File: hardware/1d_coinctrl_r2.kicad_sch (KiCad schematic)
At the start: 14 parts, among them J1 +12V INPUT, J2 CO LINE, J3 V_RLY_SEL, J5 COIN LINE, J7 Conn_01x02

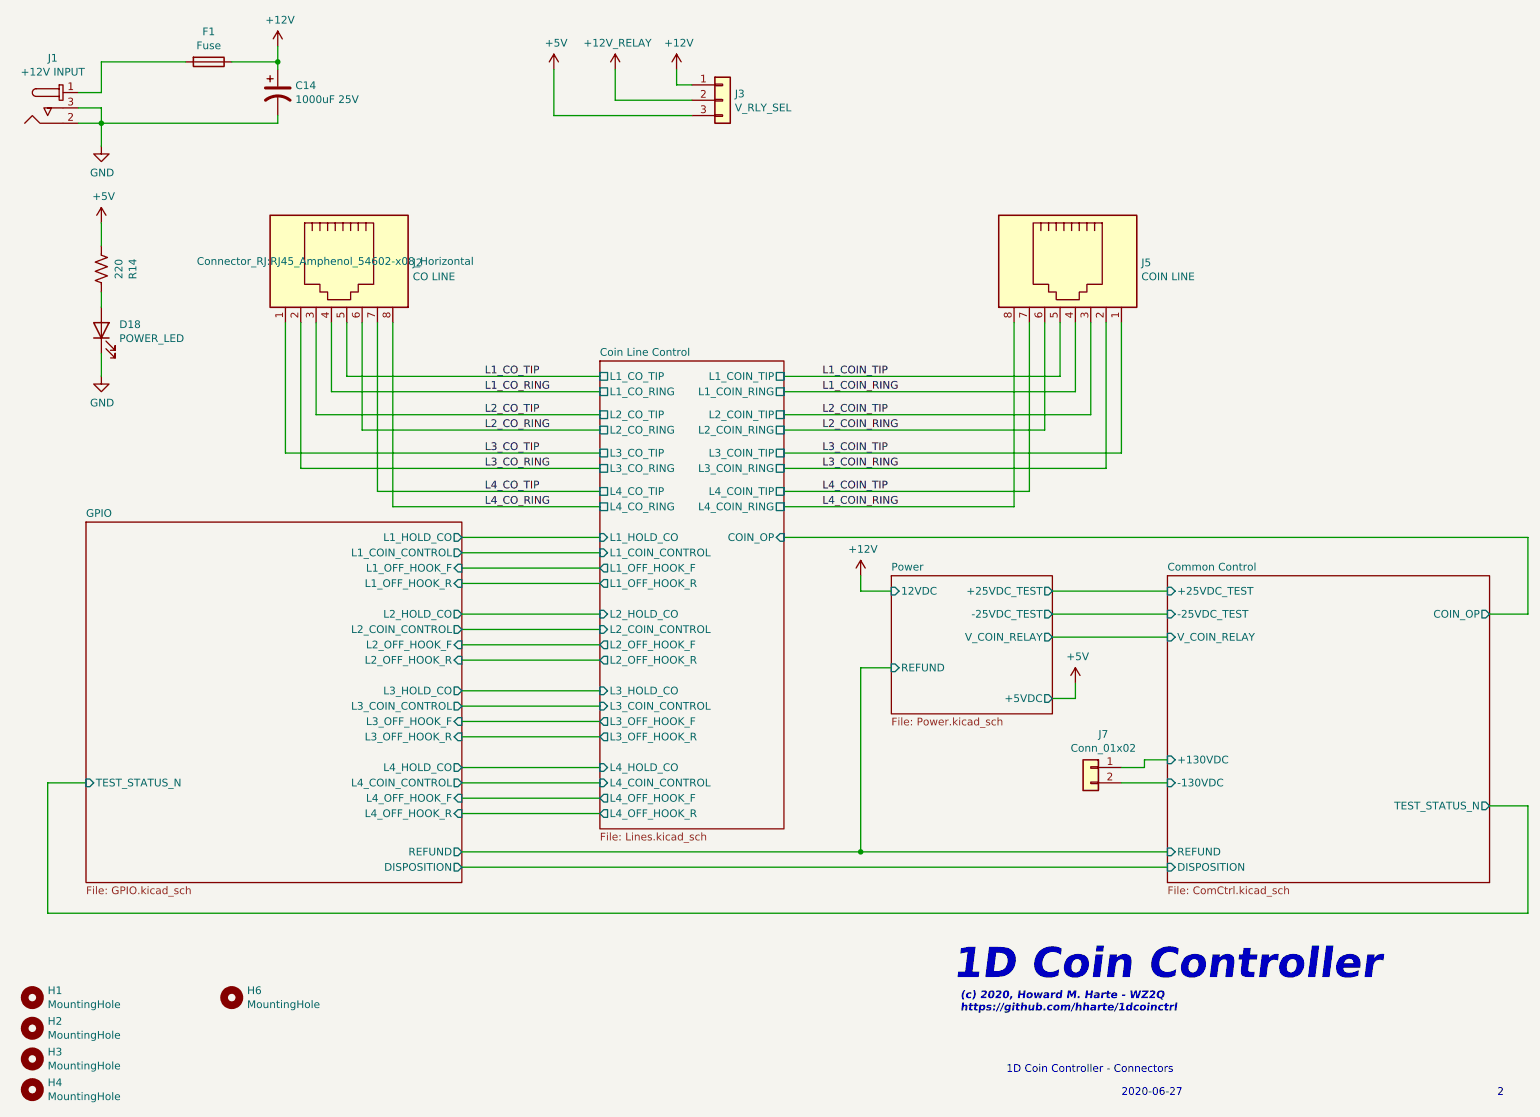
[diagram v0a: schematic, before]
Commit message: Issue 3:
* Remove barrel jack, replace with 4-position terminal block with
  provision for +/- 130VDC input in case the user already has an
  appropriate power supply and does not want the on-board
  DC-DC converter.  Note: 130V DC-DC converter PS2, relay
  K8, C14, D10, and R16 must be omitted during assembly.
* Add bi-color LEDs for line status.
  Green=Off-hook, normal polarity.
  Red=Off-hook, reverse polarity.
  Off=on-hook.
* Add header for FTDI USB UART, if user does not RS-232 UART levels.
  To use the FTDI header, do not populate U1 and other components on
  pp. 3 of the schematic.
* Remove i2c I/O expander and use PIC GPIOs directly.
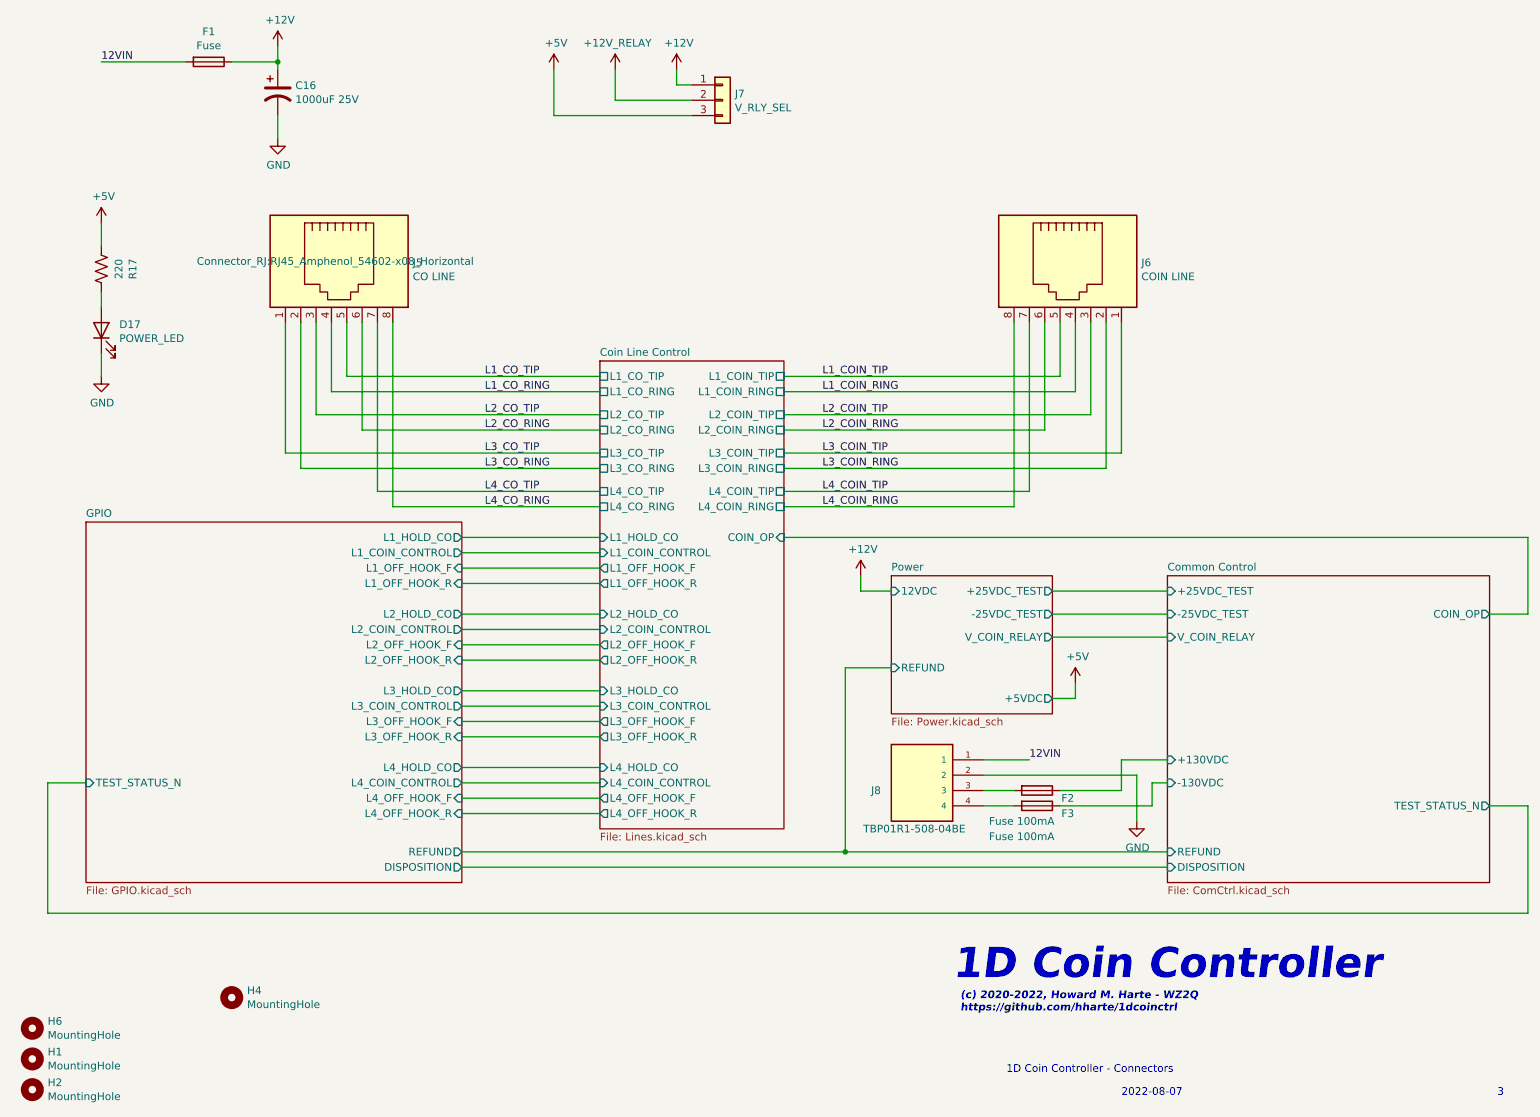
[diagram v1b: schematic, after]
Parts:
- removed H1: MountingHole, MountingHole:MountingHole_3.7mm_Pad, symbol Mechanical:MountingHole
- removed J1: +12V INPUT, digikey-footprints:Barrel_Jack_5.5mmODx2.1mmID_PJ-202A, symbol 1d_coinctrl_r2-rescue:PJ-202A-dk_Barrel-Power-Connectors
- removed J7: Conn_01x02, Connector_PinHeader_2.54mm:PinHeader_1x02_P2.54mm_Vertical, symbol Connector_Generic:Conn_01x02
- added F2, F3: Fuse 100mA, Resistor_THT:R_Axial_DIN0309_L9.0mm_D3.2mm_P12.70mm_Horizontal, symbol Device:Fuse
- added J8: TBP01R1-508-04BE, hardware:CUI_TBP01R1-508-04BE, symbol TBP01R1-508-04BE:TBP01R1-508-04BE
- renumbered C14 to C16, D18 to D17, H3 to H1, H4 to H2, H6 to H4, H2 to H6, J2 to J5, J5 to J6, J3 to J7, R14 to R17
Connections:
- net Common Control/+130VDC: now also F2.1
- net Common Control/-130VDC: now also F3.1
- net GND: now also J8.2
- net 12VIN: now reaches F1.2
- net 12VIN: now also J8.1
- new net: F3.2, J8.4
- new net: F2.2, J8.3
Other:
- note added: "(c) 2020-2022, Howard M. Harte - WZ2Q https://github.com/hharte/1dcoinctrl"
- note added: "2022-08-07"
- note added: "3"
- note removed: "(c) 2020, Howard M. Harte - WZ2Q https://github.com/hharte/1dcoinctrl"
- note removed: "2"
- note removed: "2020-06-27"
